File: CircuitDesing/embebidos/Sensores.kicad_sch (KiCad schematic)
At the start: 4 parts

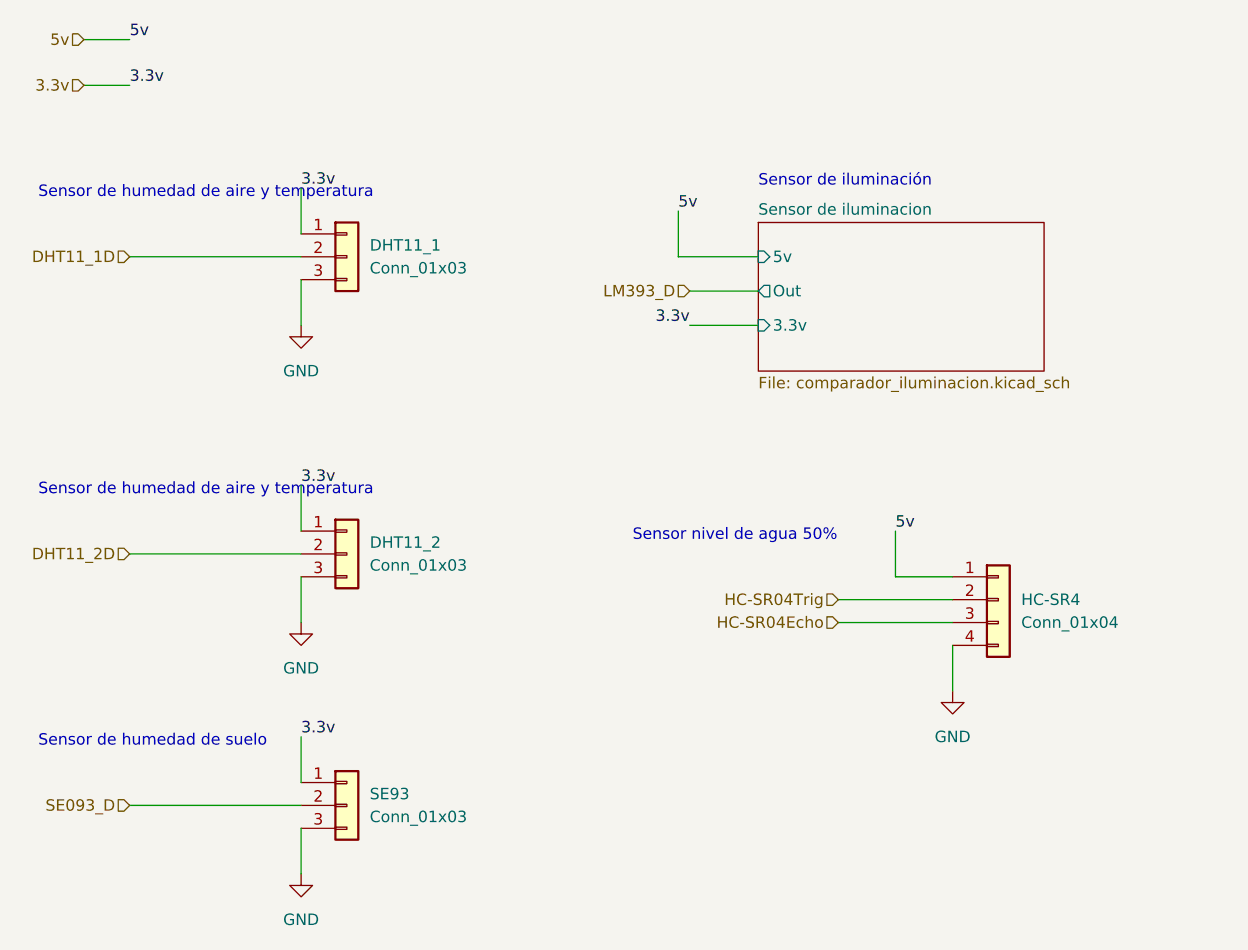
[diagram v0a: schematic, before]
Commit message: Coversores lógicos + alertas + humidificador
Coversores lógicos + alertas + humidificador
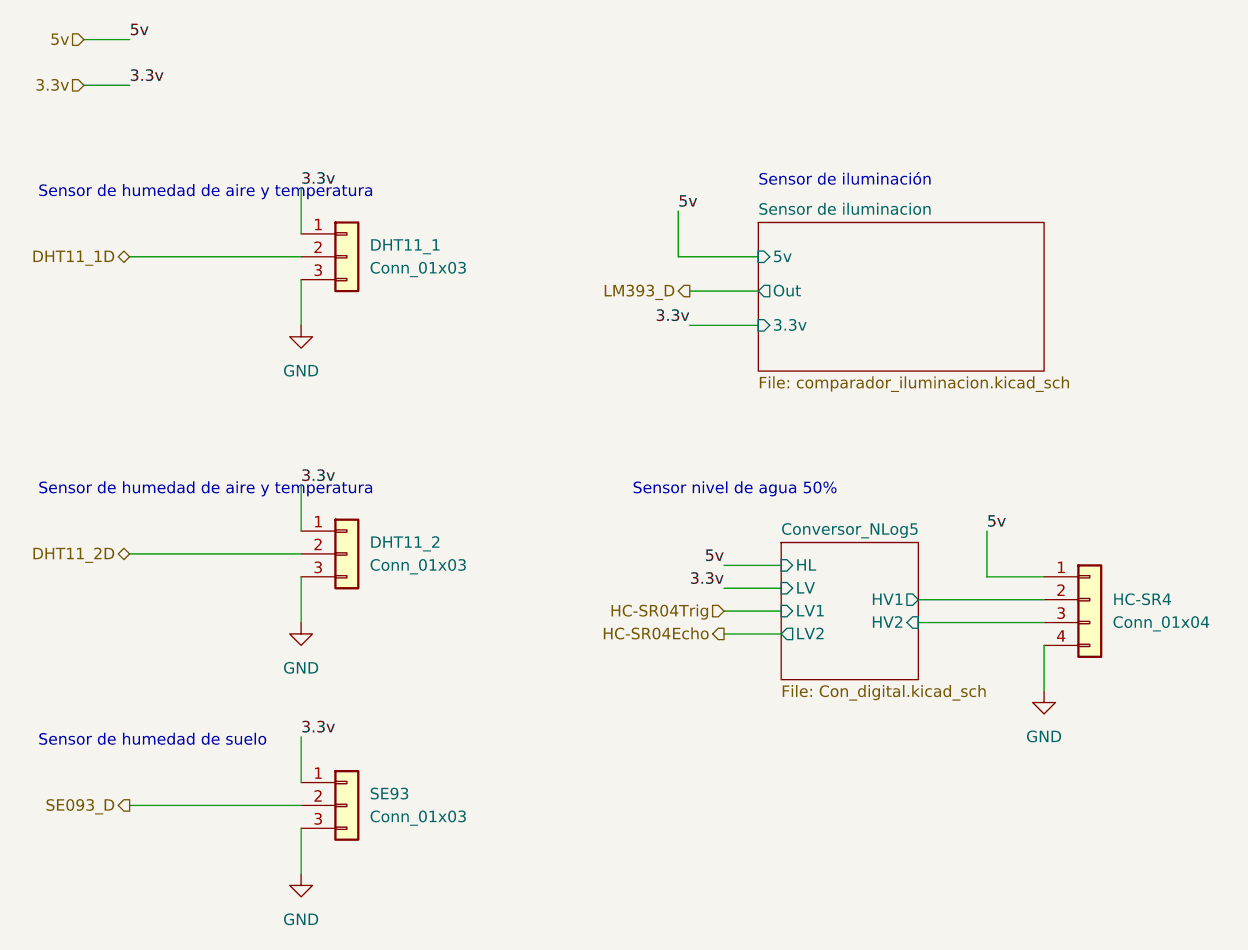
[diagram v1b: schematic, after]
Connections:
- net HC-SR04Echo: no longer HC-SR4.3 (Pin_3)
- net HC-SR04Trig: no longer HC-SR4.2 (Pin_2)
- new net Conversor_NLog5/HV1: HC-SR4.2 (Pin_2)
- new net Conversor_NLog5/HV2: HC-SR4.3 (Pin_3)
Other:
- added sheet Conversor_NLog5 (Con_digital.kicad_sch)
- moved on the sheet: HC-SR4
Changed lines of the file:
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@@
+    (stroke (width 0) (type default) (color 0 0 0 0))
+  )
+  (wire (pts (xy 116.84 101.6) (xy 123.19 101.6))
+    (stroke (width 0) (type default) (color 0 0 0 0))
+  )
+  (wire (pts (xy 116.84 99.06) (xy 123.19 99.06))
     (stroke (width 0) (type default) (color 0 0 0 0))
   )
@@
     (stroke (width 0) (type default) (color 0 0 0 0))
   )
-  (wire (pts (xy 135.89 95.25) (xy 135.89 100.33))
-    (stroke (width 0) (type default) (color 0 0 0 0))
-  )
-  (wire (pts (xy 129.54 105.41) (xy 142.24 105.41))
+  (wire (pts (xy 146.05 95.25) (xy 146.05 100.33))
     (stroke (width 0) (type default) (color 0 0 0 0))
   )
@@
     (stroke (width 0) (type default) (color 0 0 0 0))
   )
-  (wire (pts (xy 129.54 102.87) (xy 142.24 102.87))
-    (stroke (width 0) (type default) (color 0 0 0 0))
-  )
-  (wire (pts (xy 135.89 100.33) (xy 142.24 100.33))
+  (wire (pts (xy 116.84 104.14) (xy 123.19 104.14))
+    (stroke (width 0) (type default) (color 0 0 0 0))
+  )
+  (wire (pts (xy 146.05 100.33) (xy 152.4 100.33))
     (stroke (width 0) (type default) (color 0 0 0 0))
   )
@@
     (stroke (width 0) (type default) (color 0 0 0 0))
   )
-  (wire (pts (xy 142.24 107.95) (xy 142.24 113.03))
+  (wire (pts (xy 152.4 107.95) (xy 152.4 113.03))
+    (stroke (width 0) (type default) (color 0 0 0 0))
+  )
+  (wire (pts (xy 116.84 106.68) (xy 123.19 106.68))
     (stroke (width 0) (type default) (color 0 0 0 0))
   )
@@
     (stroke (width 0) (type default) (color 0 0 0 0))
   )
+  (wire (pts (xy 138.43 102.87) (xy 152.4 102.87))
+    (stroke (width 0) (type default) (color 0 0 0 0))
+  )
   (wire (pts (xy 120.65 68.58) (xy 113.03 68.58))
     (stroke (width 0) (type default) (color 0 0 0 0))
@@
     (stroke (width 0) (type default) (color 0 0 0 0))
   )
+  (wire (pts (xy 138.43 105.41) (xy 152.4 105.41))
+    (stroke (width 0) (type default) (color 0 0 0 0))
+  )
   (wire (pts (xy 113.03 72.39) (xy 120.65 72.39))
     (stroke (width 0) (type default) (color 0 0 0 0))
@@
     (effects (font (size 1.27 1.27)) (justify left bottom))
   )
-  (text "Sensor nivel de agua 50%" (at 106.68 96.52 0)
+  (text "Sensor nivel de agua 50%" (at 106.68 91.44 0)
     (effects (font (size 1.27 1.27)) (justify left bottom))
   )
@@
     (effects (font (size 1.27 1.27)) (justify left bottom))
   )
-  (label "5v" (at 135.89 95.25 0)
+  (label "3.3v" (at 116.84 101.6 180)
+    (effects (font (size 1.27 1.27)) (justify right bottom))
+  )
+  (label "5v" (at 146.05 95.25 0)
     (effects (font (size 1.27 1.27)) (justify left bottom))
   )
@@
     (effects (font (size 1.27 1.27)) (justify left bottom))
   )
+  (label "5v" (at 116.84 99.06 180)
+    (effects (font (size 1.27 1.27)) (justify right bottom))
+  )
   (label "3.3v" (at 69.85 118.11 0)
     (effects (font (size 1.27 1.27)) (justify left bottom))
   )
-  (hierarchical_label "DHT11_1D" (shape input) (at 50.8 64.77 180)
-    (effects (font (size 1.27 1.27)) (justify right))
-  )
-  (hierarchical_label "LM393_D" (shape input) (at 113.03 68.58 180)
-    (effects (font (size 1.27 1.27)) (justify right))
-  )
-  (hierarchical_label "SE093_D" (shape input) (at 50.8 125.73 180)
-    (effects (font (size 1.27 1.27)) (justify right))
-  )
-  (hierarchical_label "HC-SR04Trig" (shape input) (at 129.54 102.87 180)
+  (hierarchical_label "DHT11_1D" (shape bidirectional) (at 50.8 64.77 180)
+    (effects (font (size 1.27 1.27)) (justify right))
+  )
+  (hierarchical_label "LM393_D" (shape output) (at 113.03 68.58 180)
+    (effects (font (size 1.27 1.27)) (justify right))
+  )
+  (hierarchical_label "SE093_D" (shape output) (at 50.8 125.73 180)
     (effects (font (size 1.27 1.27)) (justify right))
   )
@@
     (effects (font (size 1.27 1.27)) (justify right))
   )
-  (hierarchical_label "HC-SR04Echo" (shape input) (at 129.54 105.41 180)
-    (effects (font (size 1.27 1.27)) (justify right))
-  )
-  (hierarchical_label "DHT11_2D" (shape input) (at 50.8 97.79 180)
-    (effects (font (size 1.27 1.27)) (justify right))
-  )
-  (symbol (lib_id "Connector_Generic:Conn_01x04") (at 147.32 102.87 0) (unit 1)
-    (in_bom yes) (on_board yes) (fields_autoplaced)
-    (property "Reference" "HC-SR4" (id 0) (at 149.86 102.8699 0)
-      (effects (font (size 1.27 1.27)) (justify left))
-    )
-    (property "Value" "Conn_01x04" (id 1) (at 149.86 105.4099 0)
-      (effects (font (size 1.27 1.27)) (justify left))
-    )
-    (property "Footprint" "Connector_JST:JST_EH_B4B-EH-A_1x04_P2.50mm_Vertical" (id 2) (at 147.32 102.87 0)
-      (effects (font (size 1.27 1.27)) hide)
-    )
-    (property "Datasheet" "~" (id 3) (at 147.32 102.87 0)
+  (hierarchical_label "HC-SR04Echo" (shape output) (at 116.84 106.68 180)
+    (effects (font (size 1.27 1.27)) (justify right))
+  )
+  (hierarchical_label "DHT11_2D" (shape bidirectional) (at 50.8 97.79 180)
+    (effects (font (size 1.27 1.27)) (justify right))
+  )
+  (hierarchical_label "HC-SR04Trig" (shape input) (at 116.84 104.14 180)
+    (effects (font (size 1.27 1.27)) (justify right))
+  )
+  (symbol (lib_id "Connector_Generic:Conn_01x04") (at 157.48 102.87 0) (unit 1)
+    (in_bom yes) (on_board yes) (fields_autoplaced)
+    (property "Reference" "HC-SR4" (id 0) (at 160.02 102.8699 0)
+      (effects (font (size 1.27 1.27)) (justify left))
+    )
+    (property "Value" "Conn_01x04" (id 1) (at 160.02 105.4099 0)
+      (effects (font (size 1.27 1.27)) (justify left))
+    )
+    (property "Footprint" "Connector_JST:JST_EH_B4B-EH-A_1x04_P2.50mm_Vertical" (id 2) (at 157.48 102.87 0)
+      (effects (font (size 1.27 1.27)) hide)
+    )
+    (property "Datasheet" "~" (id 3) (at 157.48 102.87 0)
       (effects (font (size 1.27 1.27)) hide)
     )
@@
     (pin "3")
   )
-  (symbol (lib_id "power:GND") (at 142.24 113.03 0) (unit 1)
-    (in_bom yes) (on_board yes) (fields_autoplaced)
-    (property "Reference" "#PWR05" (id 0) (at 142.24 119.38 0)
-      (effects (font (size 1.27 1.27)) hide)
-    )
-    (property "Value" "GND" (id 1) (at 142.24 118.11 0))
-    (property "Footprint" "" (id 2) (at 142.24 113.03 0)
-      (effects (font (size 1.27 1.27)) hide)
-    )
-    (property "Datasheet" "" (id 3) (at 142.24 113.03 0)
+  (symbol (lib_id "power:GND") (at 152.4 113.03 0) (unit 1)
+    (in_bom yes) (on_board yes) (fields_autoplaced)
+    (property "Reference" "#PWR05" (id 0) (at 152.4 119.38 0)
+      (effects (font (size 1.27 1.27)) hide)
+    )
+    (property "Value" "GND" (id 1) (at 152.4 118.11 0))
+    (property "Footprint" "" (id 2) (at 152.4 113.03 0)
+      (effects (font (size 1.27 1.27)) hide)
+    )
+    (property "Datasheet" "" (id 3) (at 152.4 113.03 0)
       (effects (font (size 1.27 1.27)) hide)
     )
@@
     (pin "1")
   )
+  (sheet (at 123.19 96.52) (size 15.24 15.24) (fields_autoplaced)
+    (stroke (width 0.1524) (type solid) (color 0 0 0 0))
+    (fill (color 0 0 0 0.0000))
+    (property "Sheet name" "Conversor_NLog5" (id 0) (at 123.19 95.8084 0)
+      (effects (font (size 1.27 1.27)) (justify left bottom))
+    )
+    (property "Sheet file" "Con_digital.kicad_sch" (id 1) (at 123.19 112.3446 0)
+      (effects (font (size 1.27 1.27)) (justify left top))
+    )
+    (pin "HL" input (at 123.19 99.06 180)
+      (effects (font (size 1.27 1.27)) (justify left))
+    )
+    (pin "HV1" output (at 138.43 102.87 0)
+      (effects (font (size 1.27 1.27)) (justify right))
+    )
+    (pin "LV1" input (at 123.19 104.14 180)
+      (effects (font (size 1.27 1.27)) (justify left))
+    )
+    (pin "LV" input (at 123.19 101.6 180)
+      (effects (font (size 1.27 1.27)) (justify left))
+    )
+    (pin "LV2" output (at 123.19 106.68 180)
+      (effects (font (size 1.27 1.27)) (justify left))
+    )
+    (pin "HV2" input (at 138.43 105.41 0)
+      (effects (font (size 1.27 1.27)) (justify right))
+    )
+  )
   (sheet (at 120.65 60.96) (size 31.75 16.51) (fields_autoplaced)

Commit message: Ruteo completo
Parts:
- renumbered HC-SR4 to HC-SR1, SE93 to SE1
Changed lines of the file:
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@@
   (symbol (lib_id "Connector_Generic:Conn_01x04") (at 157.48 102.87 0) (unit 1)
     (in_bom yes) (on_board yes) (fields_autoplaced)
-    (property "Reference" "HC-SR4" (id 0) (at 160.02 102.8699 0)
+    (property "Reference" "HC-SR1" (id 0) (at 160.02 102.8699 0)
       (effects (font (size 1.27 1.27)) (justify left))
     )
@@
   (symbol (lib_id "Connector_Generic:Conn_01x03") (at 74.93 125.73 0) (unit 1)
     (in_bom yes) (on_board yes) (fields_autoplaced)
-    (property "Reference" "SE93" (id 0) (at 77.47 124.4599 0)
+    (property "Reference" "SE1" (id 0) (at 77.47 124.4599 0)
       (effects (font (size 1.27 1.27)) (justify left))
     )
@@
   (symbol (lib_id "power:GND") (at 69.85 105.41 0) (unit 1)
     (in_bom yes) (on_board yes) (fields_autoplaced)
-    (property "Reference" "#PWR04" (id 0) (at 69.85 111.76 0)
+    (property "Reference" "#PWR013" (id 0) (at 69.85 111.76 0)
       (effects (font (size 1.27 1.27)) hide)
     )
@@
   (symbol (lib_id "power:GND") (at 69.85 133.35 0) (unit 1)
     (in_bom yes) (on_board yes) (fields_autoplaced)
-    (property "Reference" "#PWR06" (id 0) (at 69.85 139.7 0)
+    (property "Reference" "#PWR014" (id 0) (at 69.85 139.7 0)
       (effects (font (size 1.27 1.27)) hide)
     )
@@
   (symbol (lib_id "power:GND") (at 152.4 113.03 0) (unit 1)
     (in_bom yes) (on_board yes) (fields_autoplaced)
-    (property "Reference" "#PWR05" (id 0) (at 152.4 119.38 0)
+    (property "Reference" "#PWR015" (id 0) (at 152.4 119.38 0)
       (effects (font (size 1.27 1.27)) hide)
     )
@@
   (symbol (lib_id "power:GND") (at 69.85 72.39 0) (unit 1)
     (in_bom yes) (on_board yes) (fields_autoplaced)
-    (property "Reference" "#PWR03" (id 0) (at 69.85 78.74 0)
+    (property "Reference" "#PWR012" (id 0) (at 69.85 78.74 0)
       (effects (font (size 1.27 1.27)) hide)
     )
